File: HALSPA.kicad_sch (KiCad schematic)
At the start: 19 parts, among them J1 Conn_02x04_Odd_Even, J106 Conn_02x02_Odd_Even, J107 Conn_02x02_Odd_Even, J127 Conn_01x03, J128 Conn_01x03, J129 Conn_01x03, J130 Conn_01x03, J131 Conn_01x03, J132 Conn_01x03, J133 Conn_01x03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

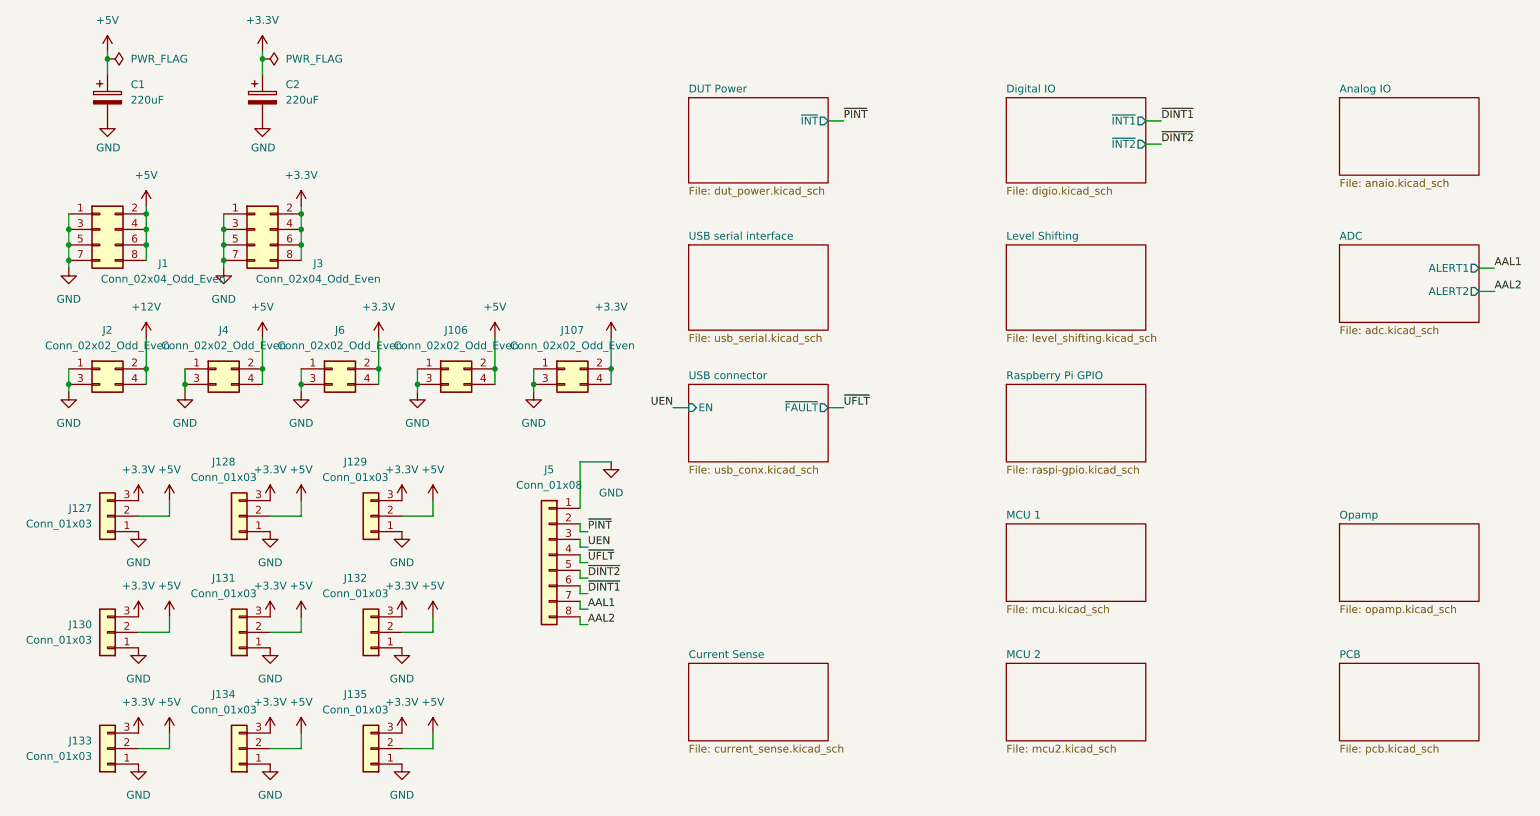
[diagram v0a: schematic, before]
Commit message: Update the design to a stackable one
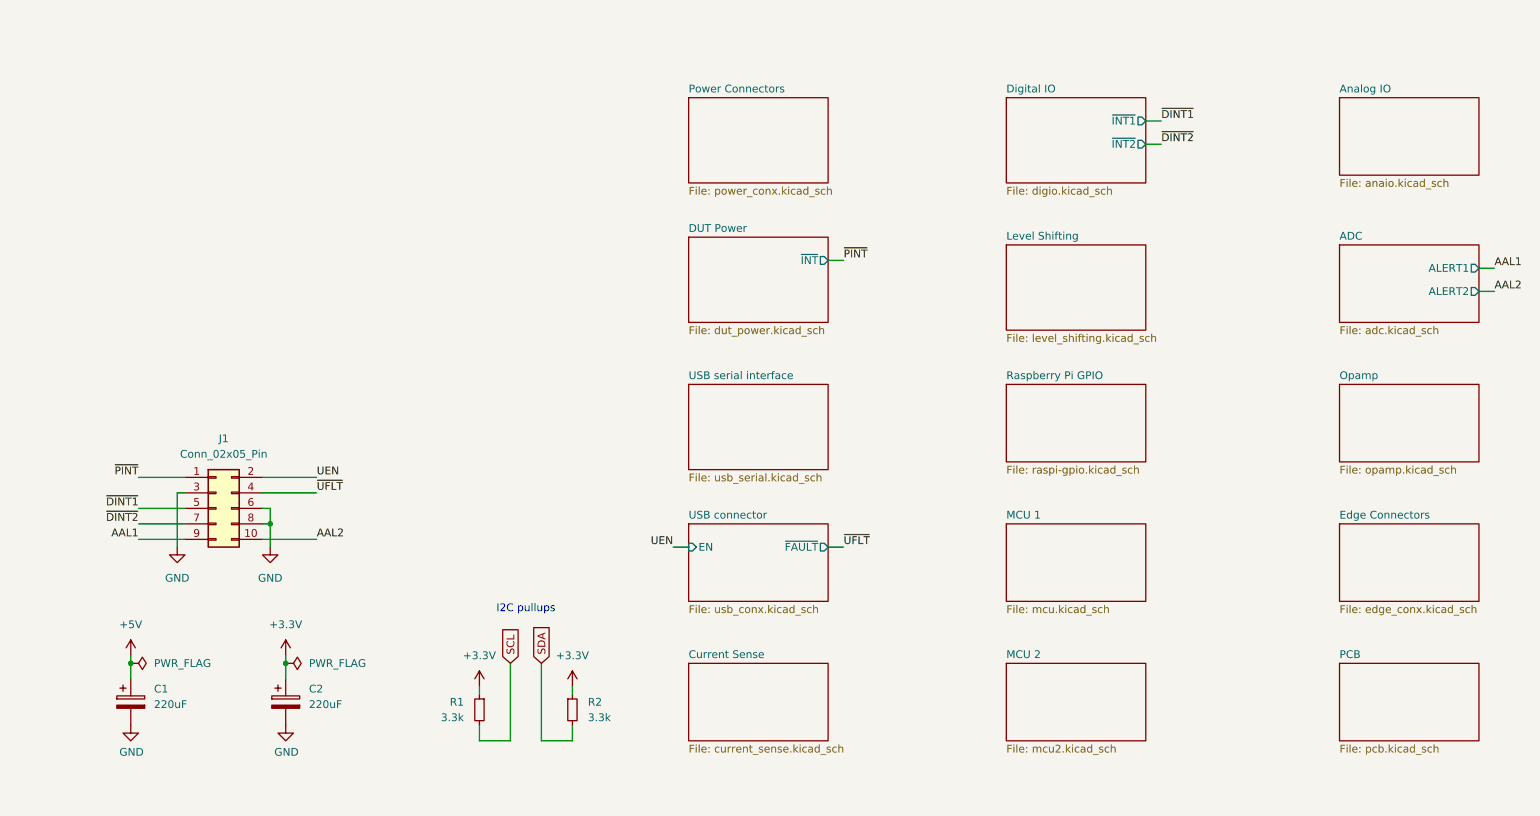
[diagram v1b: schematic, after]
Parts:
- removed J1, J3: Conn_02x04_Odd_Even, HL_Connector_Pad_2.54mm:Pad_2x04_P2.54_1.7x1.7_Rect-Rnd, symbol Connector_Generic:Conn_02x04_Odd_Even
- removed J106, J107, J2, J4, J6: Conn_02x02_Odd_Even, HL_Connector_Pad_2.54mm:Pad_2x02_P2.54_1.7x1.7_Rect-Rnd, symbol Connector_Generic:Conn_02x02_Odd_Even
- removed J127, J128, J129, J130, J131, J132, J133, J134, J135: Conn_01x03, HL_Connector_Pad_2.54mm:Pad_1x03_P2.54_1.7x1.7_Rect-2Rnd, symbol Connector_Generic:Conn_01x03
- removed J5: Conn_01x08, HL_Connector_Pad_2.54mm:Pad_1x08_P2.54_1.7x1.7_Rect-Rnd, symbol Connector_Generic:Conn_01x08
- added J1: Conn_02x05_Pin, HL_Connector_Pad_2.54mm:Pad_2x05_P2.54_1.7x1.7_2Rect-8Oct, symbol Connector_Generic:Conn_02x05_Odd_Even
- added R1, R2: 3.3k, Resistor_SMD:R_0603_1608Metric, symbol Device:R_Small
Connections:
- net +3.3V: now also R1.1, R2.1
- net AAL1: now also J1.9 (Pin_9)
- net AAL2: now also J1.10 (Pin_10)
- net GND: now also J1.3 (Pin_3), J1.6 (Pin_6), J1.8 (Pin_8)
- net UEN: now also J1.2 (Pin_2)
- net ~{DINT1}: now also J1.5 (Pin_5)
- net ~{DINT2}: now also J1.7 (Pin_7)
- net ~{PINT}: now also J1.1 (Pin_1)
- net ~{UFLT}: now also J1.4 (Pin_4)
- new net SCL: R1.2
- new net SDA: R2.2
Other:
- added sheet Edge Connectors (edge_conx.kicad_sch)
- added sheet Power Connectors (power_conx.kicad_sch)
- note added: "I2C pullups"
- moved on the sheet: C1, C2

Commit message: Edge connector changes
Probably a number of other unassorted changes as well.
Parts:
- J1: LCSC C492407 -> C492422
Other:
- removed sheet MCU 2
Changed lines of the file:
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@@
 			)
 		)
-		(property "LCSC" "C492407"
+		(property "LCSC" "C492422"
 			(at 50.8 107.95 0)
 			(effects
@@
 				)
 			)
-		)
-	)
-	(sheet
-		(at 180.34 133.35)
-		(size 22.86 12.7)
-		(exclude_from_sim no)
-		(in_bom yes)
-		(on_board yes)
-		(dnp no)
-		(fields_autoplaced yes)
-		(stroke
-			(width 0.1524)
-			(type solid)
-		)
-		(fill
-			(color 0 0 0 0.0000)
-		)
-		(property "Sheetname" "MCU 2"
-			(at 180.34 132.6384 0)
-			(effects
-				(font
-					(size 1.27 1.27)
-				)
-				(justify left bottom)
-			)
-		)
-		(property "Sheetfile" "mcu2.kicad_sch"
-			(at 180.34 146.6346 0)
-			(effects
-				(font
-					(size 1.27 1.27)
-				)
-				(justify left top)
-			)
-		)
-		(instances
-			(project "HALSPA"
-				(path "/7eeba806-440e-4671-bc07-69fe183910a7"
-					(page "23")
-				)
-			)
